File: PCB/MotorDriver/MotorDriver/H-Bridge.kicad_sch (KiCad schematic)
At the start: 9 parts, among them Q1 NMOS, Q2 NMOS, Q3 NMOS, Q4 NMOS, U1 DRV8701ERGET

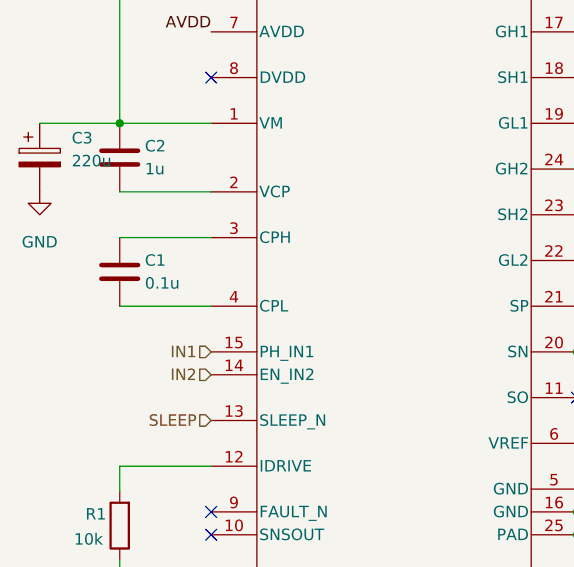
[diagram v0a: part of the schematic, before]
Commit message: Revert ":sparkles: ビアの追加"
This reverts commit f41483c75bcc19d71434e040f06f5bb4b5903eec.
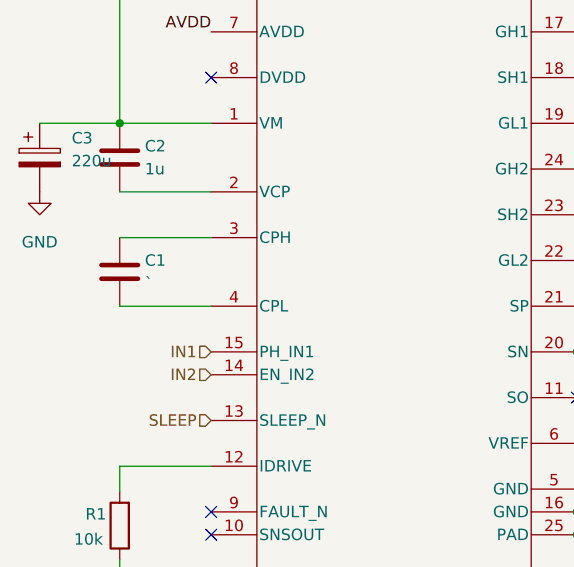
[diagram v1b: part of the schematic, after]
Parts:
- C1: value 0.1u -> `
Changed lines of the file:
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@@
           (reference "Q8") (unit 1)
-        )
-        (path "/f5374fcb-1759-4e83-8147-0b1bc8fc6833/b85d5b0f-2c56-44b1-9c6e-08bd1fa15ae1"
-          (reference "Q3") (unit 1)
         )
       )
@@
           (reference "Q6") (unit 1)
         )
-        (path "/f5374fcb-1759-4e83-8147-0b1bc8fc6833/b85d5b0f-2c56-44b1-9c6e-08bd1fa15ae1"
-          (reference "Q9") (unit 1)
-        )
       )
     )
@@
         (path "/f5374fcb-1759-4e83-8147-0b1bc8fc6833/4a280754-c36a-47c1-95c1-18daa423d0e9"
           (reference "C2") (unit 1)
-        )
-        (path "/f5374fcb-1759-4e83-8147-0b1bc8fc6833/b85d5b0f-2c56-44b1-9c6e-08bd1fa15ae1"
-          (reference "C12") (unit 1)
         )
       )
@@
           (reference "R1") (unit 1)
         )
-        (path "/f5374fcb-1759-4e83-8147-0b1bc8fc6833/b85d5b0f-2c56-44b1-9c6e-08bd1fa15ae1"
-          (reference "R3") (unit 1)
-        )
       )
     )
@@
         (path "/f5374fcb-1759-4e83-8147-0b1bc8fc6833/4a280754-c36a-47c1-95c1-18daa423d0e9"
           (reference "C3") (unit 1)
-        )
-        (path "/f5374fcb-1759-4e83-8147-0b1bc8fc6833/b85d5b0f-2c56-44b1-9c6e-08bd1fa15ae1"
-          (reference "C11") (unit 1)
         )
       )
@@
           (reference "Q5") (unit 1)
         )
-        (path "/f5374fcb-1759-4e83-8147-0b1bc8fc6833/b85d5b0f-2c56-44b1-9c6e-08bd1fa15ae1"
-          (reference "Q4") (unit 1)
-        )
       )
     )
@@
           (reference "Q7") (unit 1)
         )
-        (path "/f5374fcb-1759-4e83-8147-0b1bc8fc6833/b85d5b0f-2c56-44b1-9c6e-08bd1fa15ae1"
-          (reference "Q2") (unit 1)
-        )
       )
     )
@@
           (reference "#PWR03") (unit 1)
         )
-        (path "/f5374fcb-1759-4e83-8147-0b1bc8fc6833/b85d5b0f-2c56-44b1-9c6e-08bd1fa15ae1"
-          (reference "#PWR028") (unit 1)
-        )
       )
     )
@@
           (reference "#PWR02") (unit 1)
         )
-        (path "/f5374fcb-1759-4e83-8147-0b1bc8fc6833/b85d5b0f-2c56-44b1-9c6e-08bd1fa15ae1"
-          (reference "#PWR019") (unit 1)
-        )
       )
     )
@@
         (path "/f5374fcb-1759-4e83-8147-0b1bc8fc6833/4a280754-c36a-47c1-95c1-18daa423d0e9"
           (reference "#PWR04") (unit 1)
-        )
-        (path "/f5374fcb-1759-4e83-8147-0b1bc8fc6833/b85d5b0f-2c56-44b1-9c6e-08bd1fa15ae1"
-          (reference "#PWR020") (unit 1)
         )
       )
@@
           (reference "U1") (unit 1)
         )
-        (path "/f5374fcb-1759-4e83-8147-0b1bc8fc6833/b85d5b0f-2c56-44b1-9c6e-08bd1fa15ae1"
-          (reference "U2") (unit 1)
-        )
       )
     )
@@
           (reference "#PWR05") (unit 1)
         )
-        (path "/f5374fcb-1759-4e83-8147-0b1bc8fc6833/b85d5b0f-2c56-44b1-9c6e-08bd1fa15ae1"
-          (reference "#PWR021") (unit 1)
-        )
       )
     )
@@
       (effects (font (size 1.27 1.27)) (justify left))
     )
-    (property "Value" "0.1u" (at 56.134 81.28 0)
+    (property "Value" "`" (at 56.134 81.28 0)
       (effects (font (size 1.27 1.27)) (justify left))
     )
@@
           (reference "C1") (unit 1)
         )
-        (path "/f5374fcb-1759-4e83-8147-0b1bc8fc6833/b85d5b0f-2c56-44b1-9c6e-08bd1fa15ae1"
-          (reference "C17") (unit 1)
-        )
       )
     )
@@
           (reference "#PWR06") (unit 1)
         )
-        (path "/f5374fcb-1759-4e83-8147-0b1bc8fc6833/b85d5b0f-2c56-44b1-9c6e-08bd1fa15ae1"
-          (reference "#PWR022") (unit 1)
-        )
-      )
+      )

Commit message: :sparkles: 基板V2完成！！！
MotorDriverになってるけど普通にMain PCB V2ですわ！
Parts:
- C1: value ` -> 0.1u
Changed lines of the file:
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@@
           (reference "Q8") (unit 1)
+        )
+        (path "/f5374fcb-1759-4e83-8147-0b1bc8fc6833/b85d5b0f-2c56-44b1-9c6e-08bd1fa15ae1"
+          (reference "Q3") (unit 1)
         )
       )
@@
           (reference "Q6") (unit 1)
         )
+        (path "/f5374fcb-1759-4e83-8147-0b1bc8fc6833/b85d5b0f-2c56-44b1-9c6e-08bd1fa15ae1"
+          (reference "Q9") (unit 1)
+        )
       )
     )
@@
         (path "/f5374fcb-1759-4e83-8147-0b1bc8fc6833/4a280754-c36a-47c1-95c1-18daa423d0e9"
           (reference "C2") (unit 1)
+        )
+        (path "/f5374fcb-1759-4e83-8147-0b1bc8fc6833/b85d5b0f-2c56-44b1-9c6e-08bd1fa15ae1"
+          (reference "C12") (unit 1)
         )
       )
@@
           (reference "R1") (unit 1)
         )
+        (path "/f5374fcb-1759-4e83-8147-0b1bc8fc6833/b85d5b0f-2c56-44b1-9c6e-08bd1fa15ae1"
+          (reference "R3") (unit 1)
+        )
       )
     )
@@
         (path "/f5374fcb-1759-4e83-8147-0b1bc8fc6833/4a280754-c36a-47c1-95c1-18daa423d0e9"
           (reference "C3") (unit 1)
+        )
+        (path "/f5374fcb-1759-4e83-8147-0b1bc8fc6833/b85d5b0f-2c56-44b1-9c6e-08bd1fa15ae1"
+          (reference "C11") (unit 1)
         )
       )
@@
           (reference "Q5") (unit 1)
         )
+        (path "/f5374fcb-1759-4e83-8147-0b1bc8fc6833/b85d5b0f-2c56-44b1-9c6e-08bd1fa15ae1"
+          (reference "Q4") (unit 1)
+        )
       )
     )
@@
           (reference "Q7") (unit 1)
         )
+        (path "/f5374fcb-1759-4e83-8147-0b1bc8fc6833/b85d5b0f-2c56-44b1-9c6e-08bd1fa15ae1"
+          (reference "Q2") (unit 1)
+        )
       )
     )
@@
           (reference "#PWR03") (unit 1)
         )
+        (path "/f5374fcb-1759-4e83-8147-0b1bc8fc6833/b85d5b0f-2c56-44b1-9c6e-08bd1fa15ae1"
+          (reference "#PWR028") (unit 1)
+        )
       )
     )
@@
           (reference "#PWR02") (unit 1)
         )
+        (path "/f5374fcb-1759-4e83-8147-0b1bc8fc6833/b85d5b0f-2c56-44b1-9c6e-08bd1fa15ae1"
+          (reference "#PWR019") (unit 1)
+        )
       )
     )
@@
         (path "/f5374fcb-1759-4e83-8147-0b1bc8fc6833/4a280754-c36a-47c1-95c1-18daa423d0e9"
           (reference "#PWR04") (unit 1)
+        )
+        (path "/f5374fcb-1759-4e83-8147-0b1bc8fc6833/b85d5b0f-2c56-44b1-9c6e-08bd1fa15ae1"
+          (reference "#PWR020") (unit 1)
         )
       )
@@
           (reference "U1") (unit 1)
         )
+        (path "/f5374fcb-1759-4e83-8147-0b1bc8fc6833/b85d5b0f-2c56-44b1-9c6e-08bd1fa15ae1"
+          (reference "U2") (unit 1)
+        )
       )
     )
@@
           (reference "#PWR05") (unit 1)
         )
+        (path "/f5374fcb-1759-4e83-8147-0b1bc8fc6833/b85d5b0f-2c56-44b1-9c6e-08bd1fa15ae1"
+          (reference "#PWR021") (unit 1)
+        )
       )
     )
@@
       (effects (font (size 1.27 1.27)) (justify left))
     )
-    (property "Value" "`" (at 56.134 81.28 0)
+    (property "Value" "0.1u" (at 56.134 81.28 0)
       (effects (font (size 1.27 1.27)) (justify left))
     )
@@
         (path "/f5374fcb-1759-4e83-8147-0b1bc8fc6833/4a280754-c36a-47c1-95c1-18daa423d0e9"
           (reference "C1") (unit 1)
+        )
+        (path "/f5374fcb-1759-4e83-8147-0b1bc8fc6833/b85d5b0f-2c56-44b1-9c6e-08bd1fa15ae1"
+          (reference "C17") (unit 1)
         )
       )
@@
           (reference "#PWR06") (unit 1)
         )
-      )
+        (path "/f5374fcb-1759-4e83-8147-0b1bc8fc6833/b85d5b0f-2c56-44b1-9c6e-08bd1fa15ae1"
+          (reference "#PWR022") (unit 1)
+        )
+      )

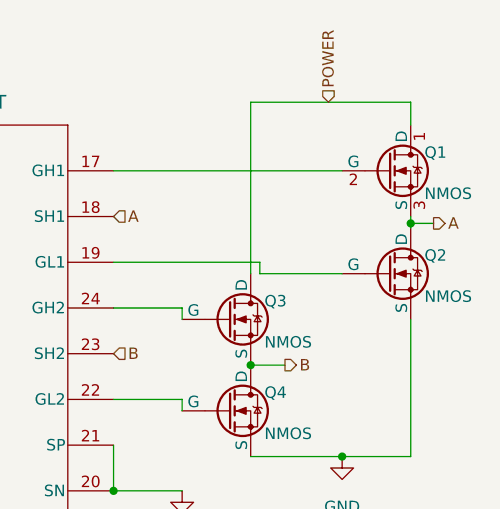
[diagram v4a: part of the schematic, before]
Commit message: ✨基板をサージに強くした
- TVSをサージ発生源に近くした
- 12Vツェナーダイオードをレギュレータの近くに取り付けた
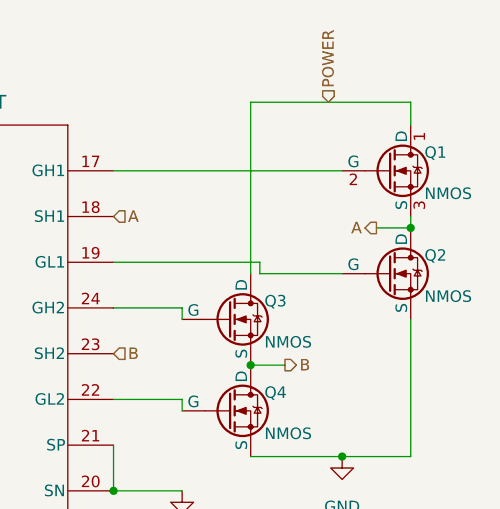
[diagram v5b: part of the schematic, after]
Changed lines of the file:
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@@
 (kicad_sch (version 20230121) (generator eeschema)
   (paper "A4")
-  (junction (at 137.16 59.182) (diameter 0) (color 0 0 0 0)
-  )
   (junction (at 104.14 109.22) (diameter 0) (color 0 0 0 0)
   )
@@
   )
   (junction (at 129.54 85.09) (diameter 0) (color 0 0 0 0)
+  )
+  (junction (at 137.16 59.69) (diameter 0) (color 0 0 0 0)
   )
   (no_connect (at 63.5 109.22))
@@
     (stroke (width 0) (type default))
   )
+  (wire (pts (xy 137.16 58.42) (xy 137.16 59.69))
+    (stroke (width 0) (type default))
+  )
   (wire (pts (xy 111.76 78.74) (xy 111.76 80.01))
     (stroke (width 0) (type default))
@@
     (stroke (width 0) (type default))
   )
-  (wire (pts (xy 137.16 59.182) (xy 139.7 59.182))
+  (wire (pts (xy 137.16 59.69) (xy 133.35 59.69))
     (stroke (width 0) (type default))
   )
@@
     (stroke (width 0) (type default))
   )
-  (wire (pts (xy 137.16 59.69) (xy 137.16 59.182))
-    (stroke (width 0) (type default))
-  )
-  (wire (pts (xy 137.16 58.42) (xy 137.16 59.182))
-    (stroke (width 0) (type default))
-  )
   (wire (pts (xy 104.14 104.14) (xy 104.14 106.68))
     (stroke (width 0) (type default))
@@
     (effects (font (size 1.27 1.27)) (justify right))
   )
-  (hierarchical_label "A" (shape output) (at 139.7 59.182 0) (fields_autoplaced)
-    (effects (font (size 1.27 1.27)) (justify left))
+  (hierarchical_label "A" (shape output) (at 133.35 59.69 180) (fields_autoplaced)
+    (effects (font (size 1.27 1.27)) (justify right))
   )
   (hierarchical_label "B" (shape input) (at 104.14 73.66 0) (fields_autoplaced)
